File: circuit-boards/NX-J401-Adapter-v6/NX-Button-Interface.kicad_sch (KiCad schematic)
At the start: 3 parts, among them J12 NX CONTROL & UART, J13 NX BUTTON

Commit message: WIP update
Signed-off-by: Scott Berman <sgberman1@gmail.com>
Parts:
- removed J13: NX BUTTON, NX-J401-Adapter:Molex-878321010, symbol Connector_Generic:Conn_02x05_Odd_Even
- added J13: NX CONTROL & UART, Connector_PinSocket_2.54mm:PinSocket_1x18_P2.54mm_Vertical, symbol Connector:Conn_01x18_Socket
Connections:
- net 3V3_BTN: now also J13.4 (Pin_4)
- net CAN_RX: now also J13.2 (Pin_2)
- net CAN_TX: now also J13.1 (Pin_1)
- net GND_BTN: now also J13.13 (Pin_13), J13.15 (Pin_15), J13.3 (Pin_3)
- net NX_PC_LED+: now also J13.8 (Pin_8)
- net NX_PC_LED-: now also J13.7 (Pin_7)
- net UART2_RXD: now also J13.9 (Pin_9)
- net UART2_TXD: now also J13.10 (Pin_10)
- net ~{REC}: now also J13.16 (Pin_16)
- net ~{SYS_RESET}: now also J13.14 (Pin_14)
- no-connect marks 6 -> 12

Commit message: Initial complete routing
Signed-off-by: Scott Berman <sgberman1@gmail.com>
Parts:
- added H5, H6: M3.7 MountingHole, MountingHole:MountingHole_3.7mm, symbol Mechanical:MountingHole
- J3: renamed from J13; KiLib_Generator (none) -> connector/pin_header_socket
- J4: renamed from J12; KiLib_Generator (none) -> connector/pin_header_socket
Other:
- note removed: "distance from Pin 15 to spacer= 0.991" pin 15 to nx-interface = 0.854" pin 15 to bottom edge of board = 0.115""
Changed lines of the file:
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@@
-		)
-	)
-	(text "distance from Pin 15 to spacer= 0.991\"\npin 15 to nx-interface = 0.854\"\npin 15 to bottom edge of board = 0.115\""
-		(exclude_from_sim no)
-		(at 221.234 152.4 0)
-		(effects
-			(font
-				(size 1.27 1.27)
-			)
-			(justify left)
 		)
 	)
@@
 		(in_pos_files yes)
 		(dnp no)
-		(property "Reference" "J12"
+		(property "Reference" "J4"
 			(at 128.27 90.17 0)
 			(show_name no)
@@
 		)
 		(property "DIST P/N" "S7016-ND"
+			(at 127 113.03 0)
+			(hide yes)
+			(show_name no)
+			(do_not_autoplace no)
+			(effects
+				(font
+					(size 1.27 1.27)
+				)
+			)
+		)
+		(property "KiLib_Generator" "connector/pin_header_socket"
 			(at 127 113.03 0)
 			(hide yes)
@@
 			(project "NX-J401-Adapter-v6"
 				(path "/3c9fa76f-2b37-4666-8575-58caa65def04/f8ff9f31-2365-4daa-ba47-54bf7f47daed"
-					(reference "J12")
+					(reference "J4")
 					(unit 1)
 				)
@@
 				(path "/cc31ce4b-09ab-4aea-a1d3-ed84696ba658/93b0701a-200b-439a-9431-66cd35259686"
 					(reference "J5")
+					(unit 1)
+				)
+			)
+		)
+	)
+	(symbol
+		(lib_id "Mechanical:MountingHole")
+		(at 217.17 102.87 0)
+		(unit 1)
+		(body_style 1)
+		(exclude_from_sim no)
+		(in_bom no)
+		(on_board yes)
+		(in_pos_files yes)
+		(dnp no)
+		(fields_autoplaced yes)
+		(property "Reference" "H5"
+			(at 219.71 101.5999 0)
+			(show_name no)
+			(do_not_autoplace no)
+			(effects
+				(font
+					(size 1.27 1.27)
+				)
+				(justify left)
+			)
+		)
+		(property "Value" "M3.7 MountingHole"
+			(at 219.71 104.1399 0)
+			(show_name no)
+			(do_not_autoplace no)
+			(effects
+				(font
+					(size 1.27 1.27)
+				)
+				(justify left)
+			)
+		)
+		(property "Footprint" "MountingHole:MountingHole_3.7mm"
+			(at 217.17 102.87 0)
+			(hide yes)
+			(show_name no)
+			(do_not_autoplace no)
+			(effects
+				(font
+					(size 1.27 1.27)
+				)
+			)
+		)
+		(property "Datasheet" ""
+			(at 217.17 102.87 0)
+			(hide yes)
+			(show_name no)
+			(do_not_autoplace no)
+			(effects
+				(font
+					(size 1.27 1.27)
+				)
+			)
+		)
+		(property "Description" "Mounting Hole without connection"
+			(at 217.17 102.87 0)
+			(hide yes)
+			(show_name no)
+			(do_not_autoplace no)
+			(effects
+				(font
+					(size 1.27 1.27)
+				)
+			)
+		)
+		(property "KiLib_Generator" "mounting_hardware/mounting_hole"
+			(at 217.17 102.87 0)
+			(hide yes)
+			(show_name no)
+			(do_not_autoplace no)
+			(effects
+				(font
+					(size 1.27 1.27)
+				)
+			)
+		)
+		(instances
+			(project "NX-J401-Adapter-v6"
+				(path "/3c9fa76f-2b37-4666-8575-58caa65def04/f8ff9f31-2365-4daa-ba47-54bf7f47daed"
+					(reference "H5")
 					(unit 1)
 				)
@@
 		(in_pos_files yes)
 		(dnp no)
-		(property "Reference" "J13"
+		(property "Reference" "J3"
 			(at 165.1 90.17 0)
 			(show_name no)
@@
 		)
 		(property "DIST P/N" "S7016-ND"
+			(at 166.37 113.03 0)
+			(hide yes)
+			(show_name no)
+			(do_not_autoplace no)
+			(effects
+				(font
+					(size 1.27 1.27)
+				)
+			)
+		)
+		(property "KiLib_Generator" "connector/pin_header_socket"
 			(at 166.37 113.03 0)
 			(hide yes)
@@
 			(project "NX-J401-Adapter-v6"
 				(path "/3c9fa76f-2b37-4666-8575-58caa65def04/f8ff9f31-2365-4daa-ba47-54bf7f47daed"
-					(reference "J13")
+					(reference "J3")
 					(unit 1)
 				)
+			)
+		)
+	)
+	(symbol
+		(lib_id "Mechanical:MountingHole")
+		(at 217.17 109.22 0)
+		(unit 1)
+		(body_style 1)
+		(exclude_from_sim no)
+		(in_bom no)
+		(on_board yes)
+		(in_pos_files yes)
+		(dnp no)
+		(fields_autoplaced yes)
+		(property "Reference" "H6"
+			(at 219.71 107.9499 0)
+			(show_name no)
+			(do_not_autoplace no)
+			(effects
+				(font
+					(size 1.27 1.27)
+				)
+				(justify left)
+			)
+		)
+		(property "Value" "M3.7 MountingHole"
+			(at 219.71 110.4899 0)
+			(show_name no)
+			(do_not_autoplace no)
+			(effects
+				(font
+					(size 1.27 1.27)
+				)
+				(justify left)
+			)
+		)
+		(property "Footprint" "MountingHole:MountingHole_3.7mm"
+			(at 217.17 109.22 0)
+			(hide yes)
+			(show_name no)
+			(do_not_autoplace no)
+			(effects
+				(font
+					(size 1.27 1.27)
+				)
+			)
+		)
+		(property "Datasheet" ""
+			(at 217.17 109.22 0)
+			(hide yes)
+			(show_name no)
+			(do_not_autoplace no)
+			(effects
+				(font
+					(size 1.27 1.27)
+				)
+			)
+		)
+		(property "Description" "Mounting Hole without connection"
+			(at 217.17 109.22 0)
+			(hide yes)
+			(show_name no)
+			(do_not_autoplace no)
+			(effects
+				(font
+					(size 1.27 1.27)
+				)
+			)
+		)
+		(property "KiLib_Generator" "mounting_hardware/mounting_hole"
+			(at 217.17 109.22 0)
+			(hide yes)
+			(show_name no)
+			(do_not_autoplace no)
+			(effects
+				(font
+					(size 1.27 1.27)
+				)
+			)
+		)
+		(instances
+			(project "NX-J401-Adapter-v6"
+				(path "/3c9fa76f-2b37-4666-8575-58caa65def04/f8ff9f31-2365-4daa-ba47-54bf7f47daed"
+					(reference "H6")
+					(unit 1)
+				)

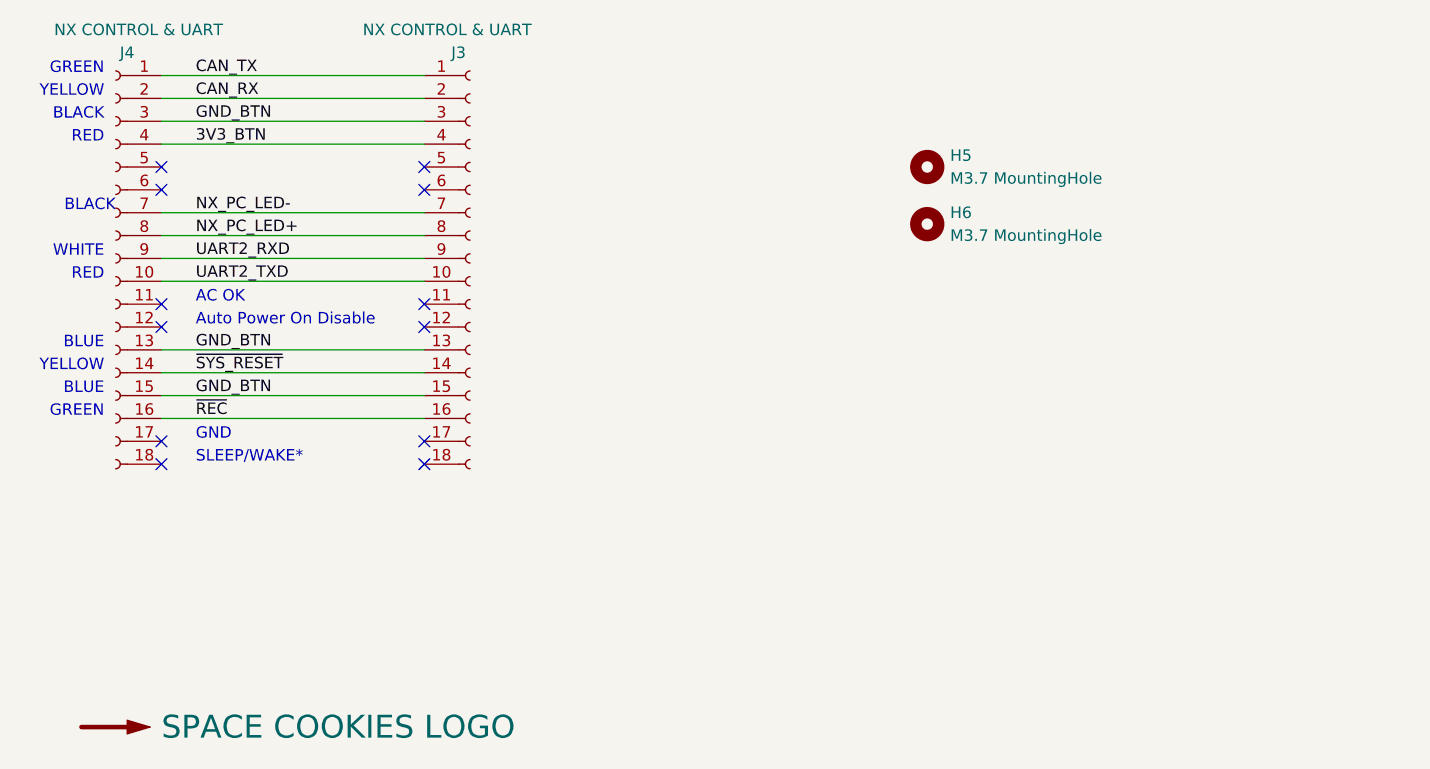
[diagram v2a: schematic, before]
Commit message: Moved the Vout connector to increase clearance
Signed-off-by: Scott Berman <sgberman1@gmail.com>
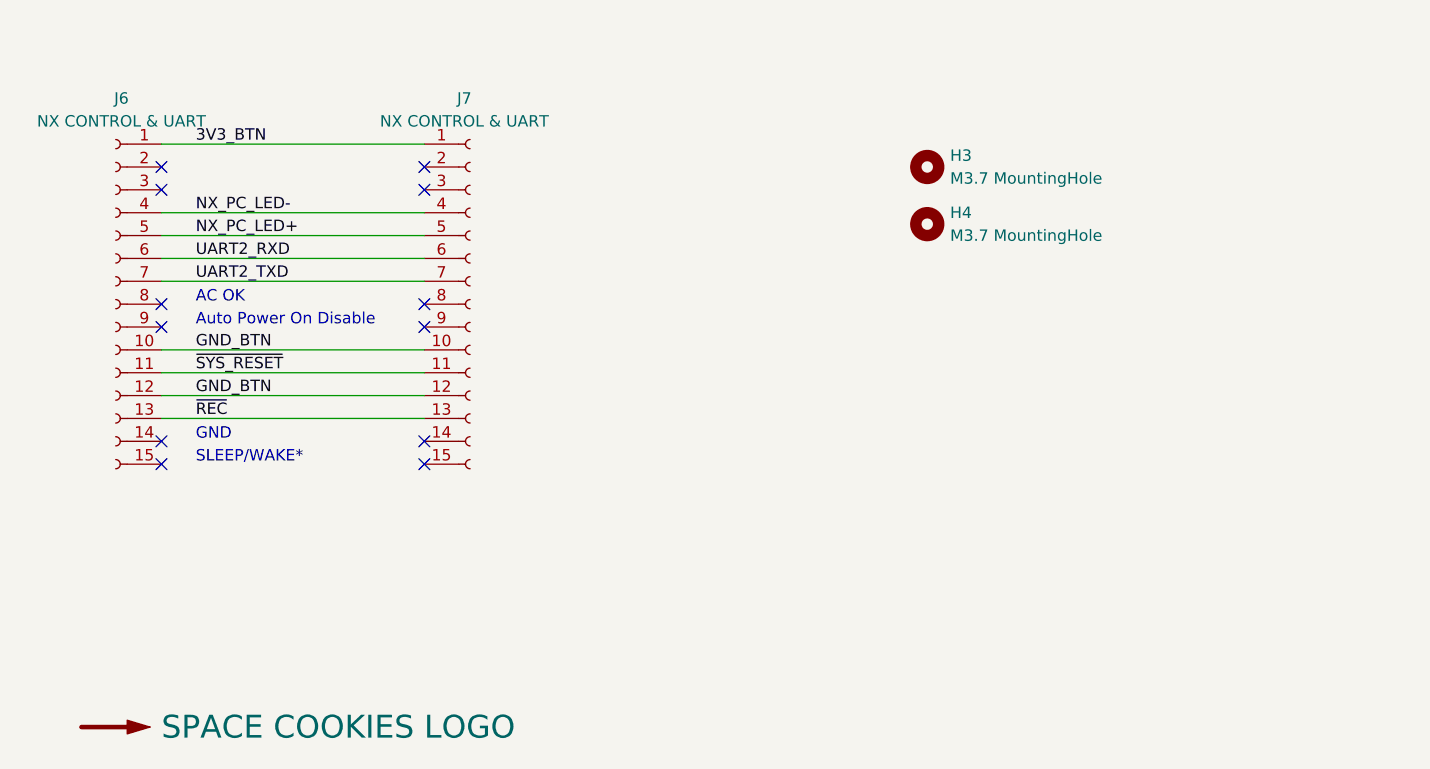
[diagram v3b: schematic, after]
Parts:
- removed J3, J4: NX CONTROL & UART, Connector_PinSocket_2.54mm:PinSocket_1x18_P2.54mm_Vertical, symbol Connector:Conn_01x18_Socket
- added J6, J7: NX CONTROL & UART, Connector_PinSocket_2.54mm:PinSocket_1x15_P2.54mm_Vertical, symbol Connector:Conn_01x15_Socket
- renumbered H5 to H3, H6 to H4
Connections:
- net 3V3_BTN: now also J6.1 (Pin_1), J7.1 (Pin_1)
- net GND_BTN: now also J6.10 (Pin_10), J6.12 (Pin_12), J7.10 (Pin_10), J7.12 (Pin_12)
- net NX_PC_LED+: now also J6.5 (Pin_5), J7.5 (Pin_5)
- net NX_PC_LED-: now also J6.4 (Pin_4), J7.4 (Pin_4)
- net UART2_RXD: now also J6.6 (Pin_6), J7.6 (Pin_6)
- net UART2_TXD: now also J6.7 (Pin_7), J7.7 (Pin_7)
- net ~{REC}: now also J6.13 (Pin_13), J7.13 (Pin_13)
- net ~{SYS_RESET}: now also J6.11 (Pin_11), J7.11 (Pin_11)
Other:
- note removed: "BLACK"
- note removed: "BLUE"
- note removed: "GREEN"
- note removed: "RED"
- note removed: "WHITE"
- note removed: "YELLOW"

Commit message: minor fixes
Signed-off-by: Scott Berman <sgberman1@gmail.com>
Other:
- company: (none) -> SPACE COOKIES FRC TEAM 1868
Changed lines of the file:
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@@
 	(title_block
 		(title "NX J401 Adapter")
-		(date "2025-11-24")
-		(rev "5")
+		(date "2026-05-25")
+		(rev "6")
+		(company "SPACE COOKIES FRC TEAM 1868")
 	)
 	(text "AC OK"

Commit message: Add rails to M.2 adapter.  Minor fixes to NX J401 adapter
Signed-off-by: Scott Berman <sgberman1@gmail.com>
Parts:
- removed LOGO1: SPACE COOKIES LOGO, NX-J401-Adapter:SPACE_COOKIES_LOGO_15mm, symbol Graphic:SYM_Arrow_Large
- added LOGO2: SPACE COOKIES LOGO, NX-J401-Adapter:SPACE_COOKIES_LOGO_7mm, symbol Graphic:SYM_Arrow_Large
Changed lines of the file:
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@@
+	)
+	(symbol
+		(lib_id "Graphic:SYM_Arrow_Large")
+		(at 217.17 151.13 0)
+		(unit 1)
+		(body_style 1)
+		(exclude_from_sim no)
+		(in_bom no)
+		(on_board yes)
+		(in_pos_files yes)
+		(dnp no)
+		(property "Reference" "LOGO2"
+			(at 217.17 148.844 0)
+			(hide yes)
+			(show_name no)
+			(do_not_autoplace no)
+			(effects
+				(font
+					(size 1.27 1.27)
+				)
+			)
+		)
+		(property "Value" "SPACE COOKIES LOGO"
+			(at 222.25 151.13 0)
+			(show_name no)
+			(do_not_autoplace no)
+			(effects
+				(font
+					(size 2.54 2.54)
+				)
+				(justify left)
+			)
+		)
+		(property "Footprint" "NX-J401-Adapter:SPACE_COOKIES_LOGO_7mm"
+			(at 217.17 151.13 0)
+			(hide yes)
+			(show_name no)
+			(do_not_autoplace no)
+			(effects
+				(font
+					(size 1.27 1.27)
+				)
+			)
+		)
+		(property "Datasheet" ""
+			(at 217.17 151.13 0)
+			(hide yes)
+			(show_name no)
+			(do_not_autoplace no)
+			(effects
+				(font
+					(size 1.27 1.27)
+				)
+			)
+		)
+		(property "Description" ""
+			(at 217.17 151.13 0)
+			(hide yes)
+			(show_name no)
+			(do_not_autoplace no)
+			(effects
+				(font
+					(size 1.27 1.27)
+				)
+			)
+		)
+		(instances
+			(project "NX-J401-Adapter-v6"
+				(path "/3c9fa76f-2b37-4666-8575-58caa65def04/f8ff9f31-2365-4daa-ba47-54bf7f47daed"
+					(reference "LOGO2")
+					(unit 1)
+				)
+			)
+		)
 	)
 	(symbol
@@
 					(unit 1)
 				)
-			)
-		)
-	)
-	(symbol
-		(lib_id "Graphic:SYM_Arrow_Large")
-		(at 127 165.1 0)
-		(unit 1)
-		(body_style 1)
-		(exclude_from_sim no)
-		(in_bom no)
-		(on_board yes)
-		(in_pos_files yes)
-		(dnp no)
-		(property "Reference" "LOGO1"
-			(at 127 162.814 0)
-			(hide yes)
-			(show_name no)
-			(do_not_autoplace no)
-			(effects
-				(font
-					(size 1.27 1.27)
-				)
-			)
-		)
-		(property "Value" "SPACE COOKIES LOGO"
-			(at 132.08 165.1 0)
-			(show_name no)
-			(do_not_autoplace no)
-			(effects
-				(font
-					(size 2.54 2.54)
-				)
-				(justify left)
-			)
-		)
-		(property "Footprint" "NX-J401-Adapter:SPACE_COOKIES_LOGO_15mm"
-			(at 127 165.1 0)
-			(hide yes)
-			(show_name no)
-			(do_not_autoplace no)
-			(effects
-				(font
-					(size 1.27 1.27)
-				)
-			)
-		)
-		(property "Datasheet" ""
-			(at 127 165.1 0)
-			(hide yes)
-			(show_name no)
-			(do_not_autoplace no)
-			(effects
-				(font
-					(size 1.27 1.27)
-				)
-			)
-		)
-		(property "Description" ""
-			(at 127 165.1 0)
-			(hide yes)
-			(show_name no)
-			(do_not_autoplace no)
-			(effects
-				(font
-					(size 1.27 1.27)
-				)
-			)
-		)
-		(instances
-			(project "NX-J401-Adapter-v6"
-				(path "/3c9fa76f-2b37-4666-8575-58caa65def04/f8ff9f31-2365-4daa-ba47-54bf7f47daed"
-					(reference "LOGO1")
-					(unit 1)
-				)
-			)
-			(project "NX-J401-Adapter"
-				(path "/cc31ce4b-09ab-4aea-a1d3-ed84696ba658/93b0701a-200b-439a-9431-66cd35259686"
-					(reference "LOGO2")
-					(unit 1)
-				)

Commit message: Updates
Signed-off-by: Scott Berman <sgberman1@gmail.com>
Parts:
- H3, H4: footprint MountingHole:MountingHole_3.7mm -> NX-J401-Adapter:MountingHole_3.7mm; symbol Mechanical:MountingHole -> NX-J401-Adapter:MountingHole
- J6, J7: footprint Connector_PinSocket_2.54mm:PinSocket_1x15_P2.54mm_Vertical -> NX-J401-Adapter:PinSocket_1x15_P2.54mm_Vertical; symbol Connector:Conn_01x15_Socket -> NX-J401-Adapter:Conn_01x15_Socket
- LOGO2: symbol Graphic:SYM_Arrow_Large -> NX-J401-Adapter:SYM_Arrow_Large
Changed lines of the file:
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@@
 	(title_block
 		(title "NX J401 Adapter")
-		(date "2026-05-25")
+		(date "2026-06-02")
 		(rev "6")
 		(company "SPACE COOKIES FRC TEAM 1868")
@@
 	)
 	(symbol
-		(lib_id "Mechanical:MountingHole")
+		(lib_id "NX-J401-Adapter:MountingHole")
 		(at 217.17 102.87 0)
 		(unit 1)
@@
 			)
 		)
-		(property "Footprint" "MountingHole:MountingHole_3.7mm"
+		(property "Footprint" "NX-J401-Adapter:MountingHole_3.7mm"
 			(at 217.17 102.87 0)
 			(hide yes)
@@
 	)
 	(symbol
-		(lib_id "Graphic:SYM_Arrow_Large")
+		(lib_id "NX-J401-Adapter:SYM_Arrow_Large")
 		(at 217.17 151.13 0)
 		(unit 1)
@@
 	)
 	(symbol
-		(lib_id "Connector:Conn_01x15_Socket")
+		(lib_id "NX-J401-Adapter:Conn_01x15_Socket")
 		(at 127 118.11 0)
 		(mirror y)
@@
 			)
 		)
-		(property "Footprint" "Connector_PinSocket_2.54mm:PinSocket_1x15_P2.54mm_Vertical"
+		(property "Footprint" "NX-J401-Adapter:PinSocket_1x15_P2.54mm_Vertical"
 			(at 127 118.11 0)
 			(hide yes)
@@
 	)
 	(symbol
-		(lib_id "Connector:Conn_01x15_Socket")
+		(lib_id "NX-J401-Adapter:Conn_01x15_Socket")
 		(at 166.37 118.11 0)
 		(unit 1)
@@
 			)
 		)
-		(property "Footprint" "Connector_PinSocket_2.54mm:PinSocket_1x15_P2.54mm_Vertical"
+		(property "Footprint" "NX-J401-Adapter:PinSocket_1x15_P2.54mm_Vertical"
 			(at 166.37 118.11 0)
 			(hide yes)
@@
 	)
 	(symbol
-		(lib_id "Mechanical:MountingHole")
+		(lib_id "NX-J401-Adapter:MountingHole")
 		(at 217.17 109.22 0)
 		(unit 1)
@@
 			)
 		)
-		(property "Footprint" "MountingHole:MountingHole_3.7mm"
+		(property "Footprint" "NX-J401-Adapter:MountingHole_3.7mm"
 			(at 217.17 109.22 0)
 			(hide yes)

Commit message: Adjusted connector positioning to more closely match J401.
Signed-off-by: Scott Berman <sgberman1@gmail.com>
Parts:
- renumbered H3 to H4, H4 to H6, J6 to J5, J7 to J6
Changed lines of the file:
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@@
 		(dnp no)
 		(fields_autoplaced yes)
-		(property "Reference" "H3"
+		(property "Reference" "H4"
 			(at 219.71 101.5999 0)
 			(show_name no)
@@
 			(project "NX-J401-Adapter-v6"
 				(path "/3c9fa76f-2b37-4666-8575-58caa65def04/f8ff9f31-2365-4daa-ba47-54bf7f47daed"
-					(reference "H3")
+					(reference "H4")
 					(unit 1)
 				)
@@
 		(dnp no)
 		(fields_autoplaced yes)
-		(property "Reference" "J6"
+		(property "Reference" "J5"
 			(at 127.635 95.25 0)
 			(show_name no)
@@
 			(project "NX-J401-Adapter-v6"
 				(path "/3c9fa76f-2b37-4666-8575-58caa65def04/f8ff9f31-2365-4daa-ba47-54bf7f47daed"
-					(reference "J6")
+					(reference "J5")
 					(unit 1)
 				)
@@
 		(in_pos_files yes)
 		(dnp no)
-		(property "Reference" "J7"
+		(property "Reference" "J6"
 			(at 165.735 95.25 0)
 			(show_name no)
@@
 			(project "NX-J401-Adapter-v6"
 				(path "/3c9fa76f-2b37-4666-8575-58caa65def04/f8ff9f31-2365-4daa-ba47-54bf7f47daed"
-					(reference "J7")
+					(reference "J6")
 					(unit 1)
 				)
@@
 		(dnp no)
 		(fields_autoplaced yes)
-		(property "Reference" "H4"
+		(property "Reference" "H6"
 			(at 219.71 107.9499 0)
 			(show_name no)
@@
 			(project "NX-J401-Adapter-v6"
 				(path "/3c9fa76f-2b37-4666-8575-58caa65def04/f8ff9f31-2365-4daa-ba47-54bf7f47daed"
-					(reference "H4")
+					(reference "H6")
 					(unit 1)
 				)
